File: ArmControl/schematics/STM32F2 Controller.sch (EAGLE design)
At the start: 87 parts, among them IC1 REG1117, IC2 TL072D, IC3 TL072D, Q301 BC846, Q701 BC846, U1 STM32F10XRXT6

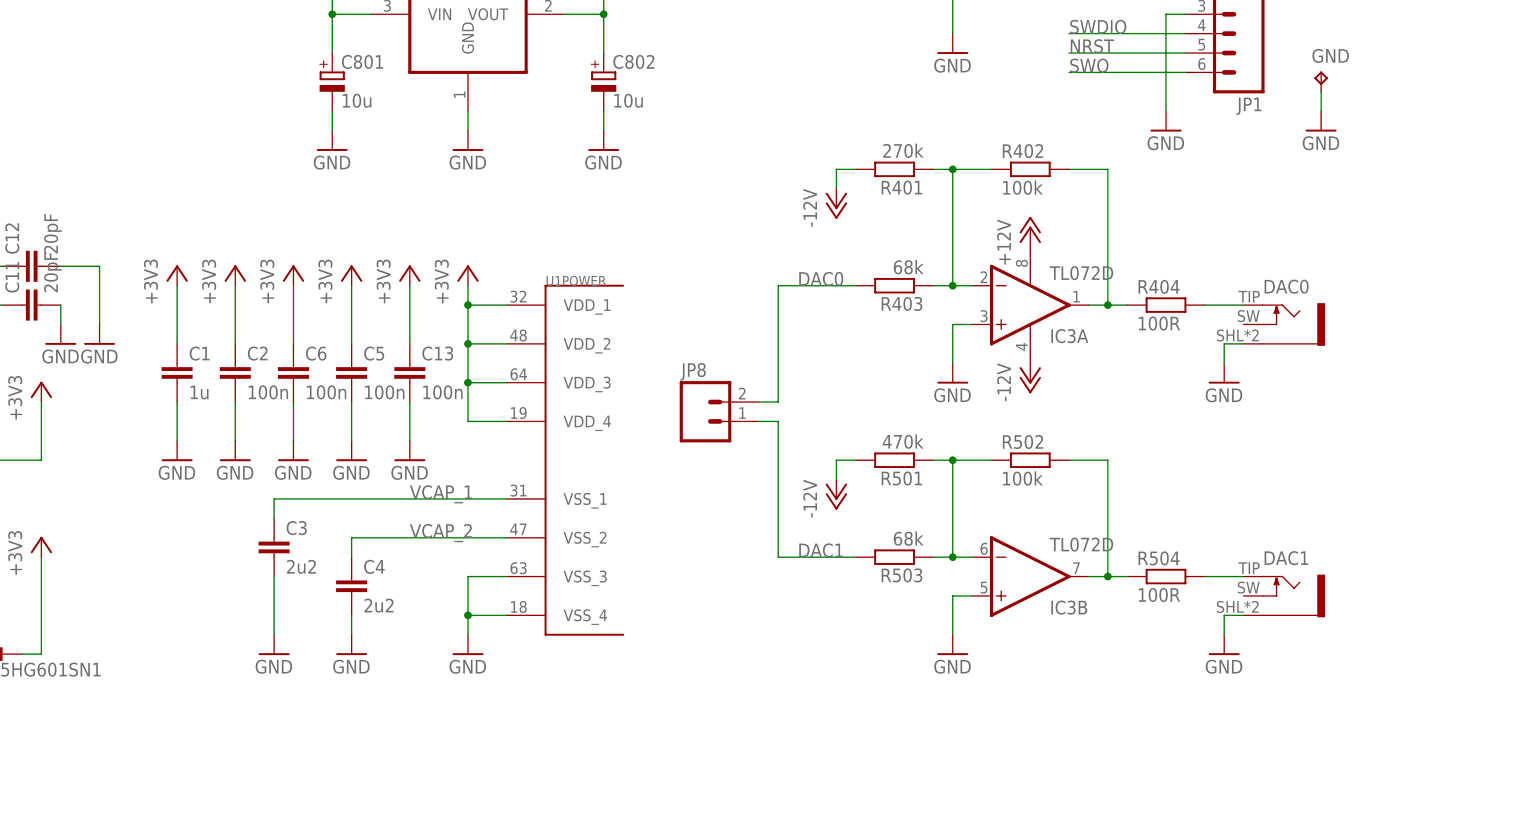
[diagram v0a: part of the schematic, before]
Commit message: rerouted pc0-pc3
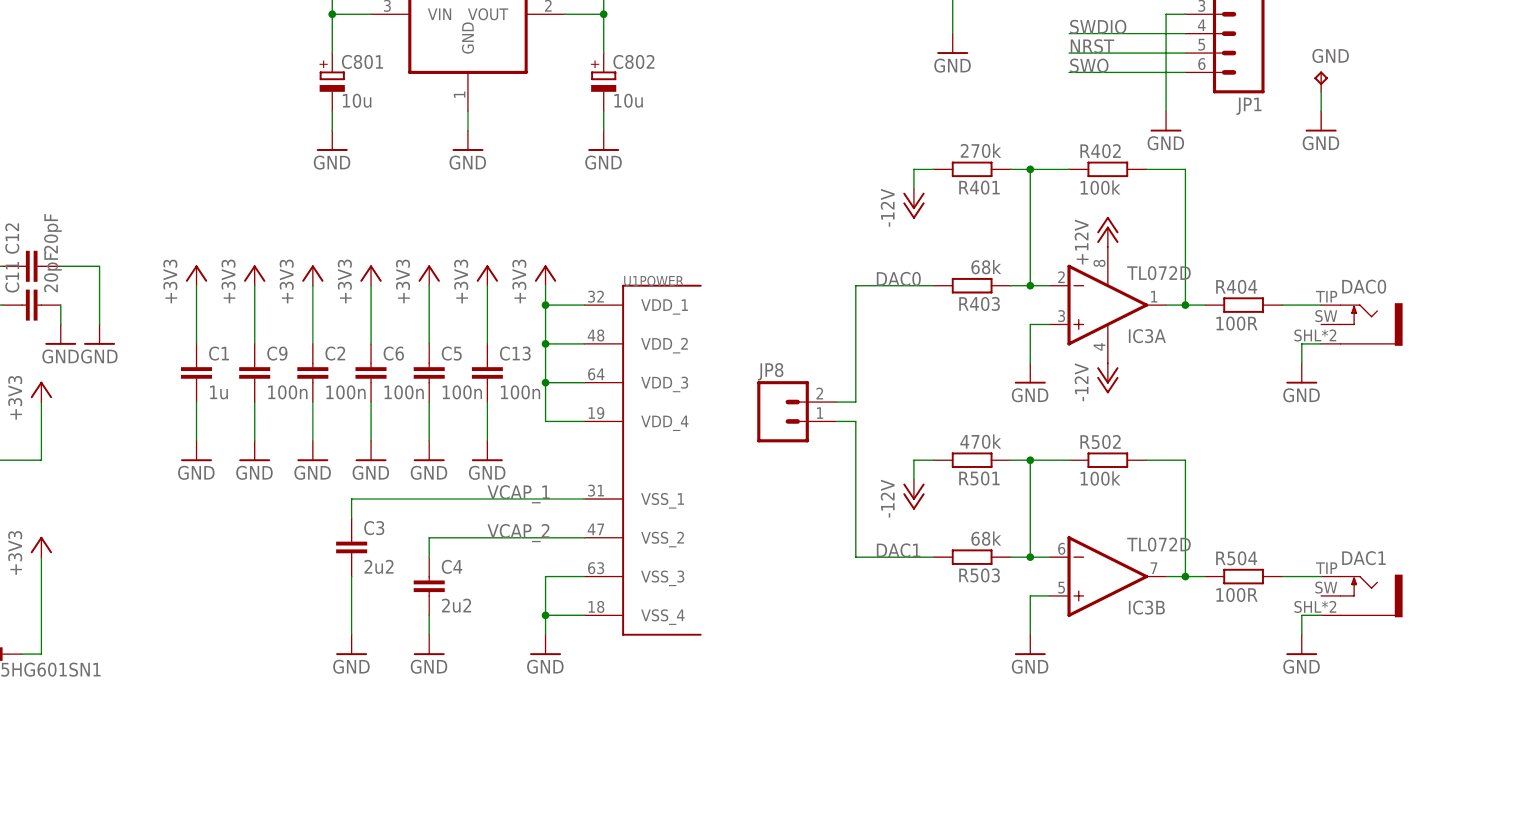
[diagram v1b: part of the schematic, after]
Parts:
- added C9: 100n, resistor:C-EUC0603
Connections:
- net +3V3: now also C9.1
- net GND: now also C9.2
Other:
- moved on the sheet: C1, C13, C2, C3, C4, C5, C6, DAC0, DAC1, IC3A, IC3B, JP8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

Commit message: removed usb connector, inserted jack headers, routed
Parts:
- removed D801: (no value), SparkFun:DIODESMA
- removed GND: TPPAD1-20, testpad:TPPAD1-20
- removed R801, R802: 22R, resistor:R-EU_R0603
- removed R803: 100k, resistor:R-EU_R0603
- removed U$3: USB-MINIB-5PIN, SparkFun:USB-MINIB-5PIN
- added JP11, JP12, JP13, JP14, JP15, JP16, JP17, JP18, JP19, JP20, JP21, JP22, JP23: (no value), SparkFun:M02PTH
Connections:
- removed net DM: R801.1, U$3.D-
- removed net DP: R802.1, U$3.D+
- new net N$10: DGO0.SW, JP11.1
- new net N$11: DGO0.TIP, JP11.2
- new net N$22: DGI0.SW, JP14.1
- new net N$23: DGI0.TIP, JP14.2
- new net N$24: ADC1.SW, JP16.1
- new net N$25: ADC1.TIP, JP16.2
- new net N$26: JP17.2, R203.1
- new net N$29: DAC1.SW, JP20.1
- new net N$30: DAC1.TIP, JP20.2
- new net N$31: JP18.1, R404.2
- new net N$32: JP18.2, R504.2
- net +12V: now also JP23.1
- net +3V3: now also JP21.1
- net +5V: now also JP22.1; no longer D801.C
- net -12V: now also JP23.2
- net DI0: now also JP12.2
- net DO0: now also JP13.1
- net GND: now also JP21.2, JP22.2; no longer ADC0.SW, ADC1.SW, DGI0.SW, GND.TP, R803.2, U$3.GND, U$3.MTN1, U$3.MTN2, U$3.MTN3, U$3.MTN4
- net N$1: now also ADC0.SW, JP15.1; no longer ADC1.TIP, R103.1
- net N$17: now also JP15.2; no longer R203.1
- net N$21: now also JP12.1, R301.1; no longer R803.1, U$3.ID
- net N$28: now also JP17.1, R103.1; no longer DGI0.TIP, R301.1
- net N$35: now also JP13.2; no longer DGO0.TIP
- net N$8: now also DAC0.SW, JP19.1; no longer DAC0.TIP, R404.2
- net N$9: now also DAC0.TIP, JP19.2; no longer DAC1.TIP, R504.2
- net PA11: no longer R801.2
- net PA12: no longer R802.2
- net PA9: no longer D801.A, U$3.VBUS
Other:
- moved on the sheet: ADC0, ADC1, DAC0, DAC1, DGI0, DGO0

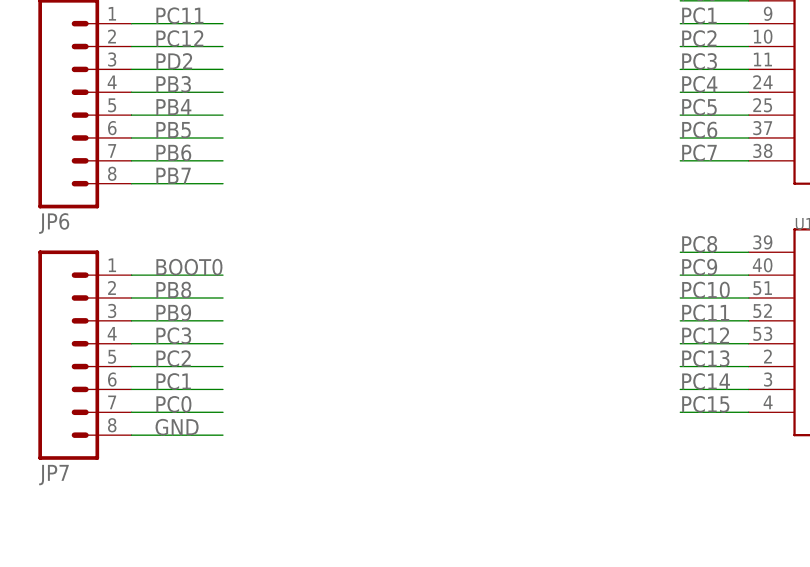
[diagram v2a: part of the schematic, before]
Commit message: added header for PC13-PC15
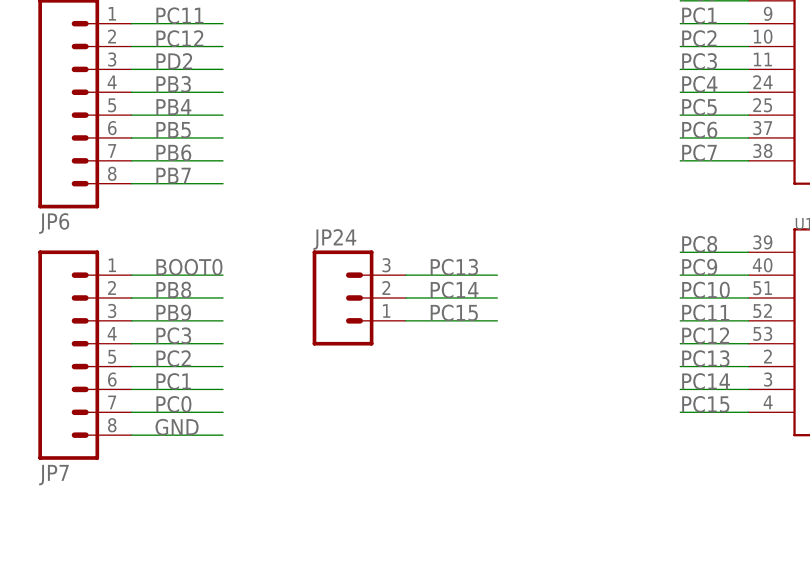
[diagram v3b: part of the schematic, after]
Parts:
- added JP24: (no value), SparkFun:M03PTH
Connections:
- net PC13: now also JP24.3
- net PC14: now also JP24.2
- net PC15: now also JP24.1
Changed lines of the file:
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@@
 <part name="P-8" library="supply1" deviceset="-12V" device=""/>
 <part name="P+8" library="supply1" deviceset="+12V" device=""/>
+<part name="JP24" library="SparkFun" deviceset="M03" device="PTH"/>
 </parts>
 <sheets>
@@
 <instance part="P-8" gate="1" x="355.6" y="55.88"/>
 <instance part="P+8" gate="1" x="355.6" y="73.66"/>
+<instance part="JP24" gate="G$1" x="-7.62" y="-17.78"/>
 </instances>
 <busses>
@@
 <pinref part="U1" gate="PORTC_H" pin="PC13"/>
 </segment>
+<segment>
+<pinref part="JP24" gate="G$1" pin="3"/>
+<wire x1="0" y1="-15.24" x2="10.16" y2="-15.24" width="0.1524" layer="91"/>
+<label x="2.54" y="-15.24" size="1.778" layer="95"/>
+</segment>
 </net>
 <net name="PC15" class="0">
@@
 <label x="30.48" y="-30.48" size="1.778" layer="95"/>
 <pinref part="U1" gate="PORTC_H" pin="PC15"/>
+</segment>
+<segment>
+<pinref part="JP24" gate="G$1" pin="1"/>
+<wire x1="0" y1="-20.32" x2="10.16" y2="-20.32" width="0.1524" layer="91"/>
+<label x="2.54" y="-20.32" size="1.778" layer="95"/>
 </segment>
 </net>
@@
 <pinref part="U1" gate="PORTC_H" pin="PC14"/>
 </segment>
-</net>
+<segment>
+<pinref part="JP24" gate="G$1" pin="2"/>
+<wire x1="0" y1="-17.78" x2="10.16" y2="-17.78" width="0.1524" layer="91"/>
+<label x="2.54" y="-17.78" size="1.778" layer="95"/>
+</segment>
+</net>

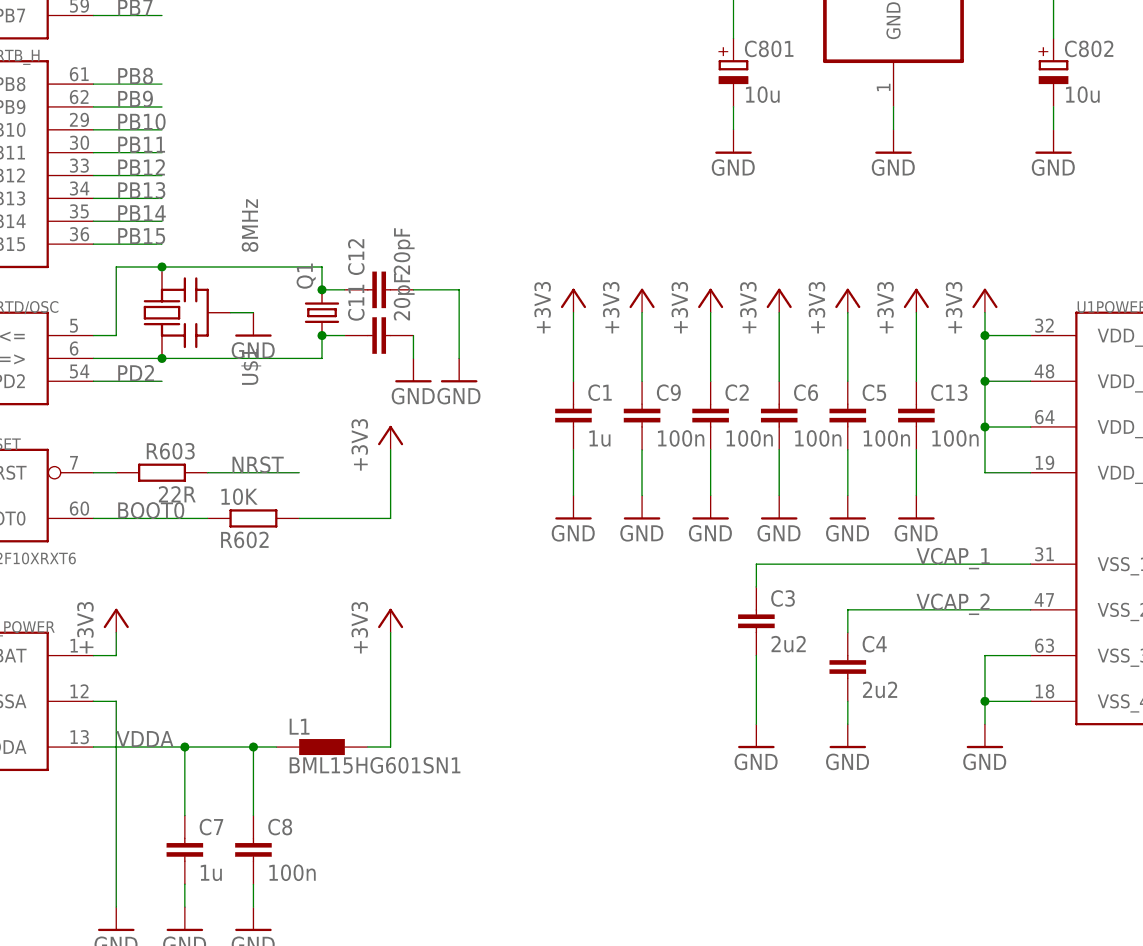
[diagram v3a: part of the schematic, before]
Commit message: added and layed out labels
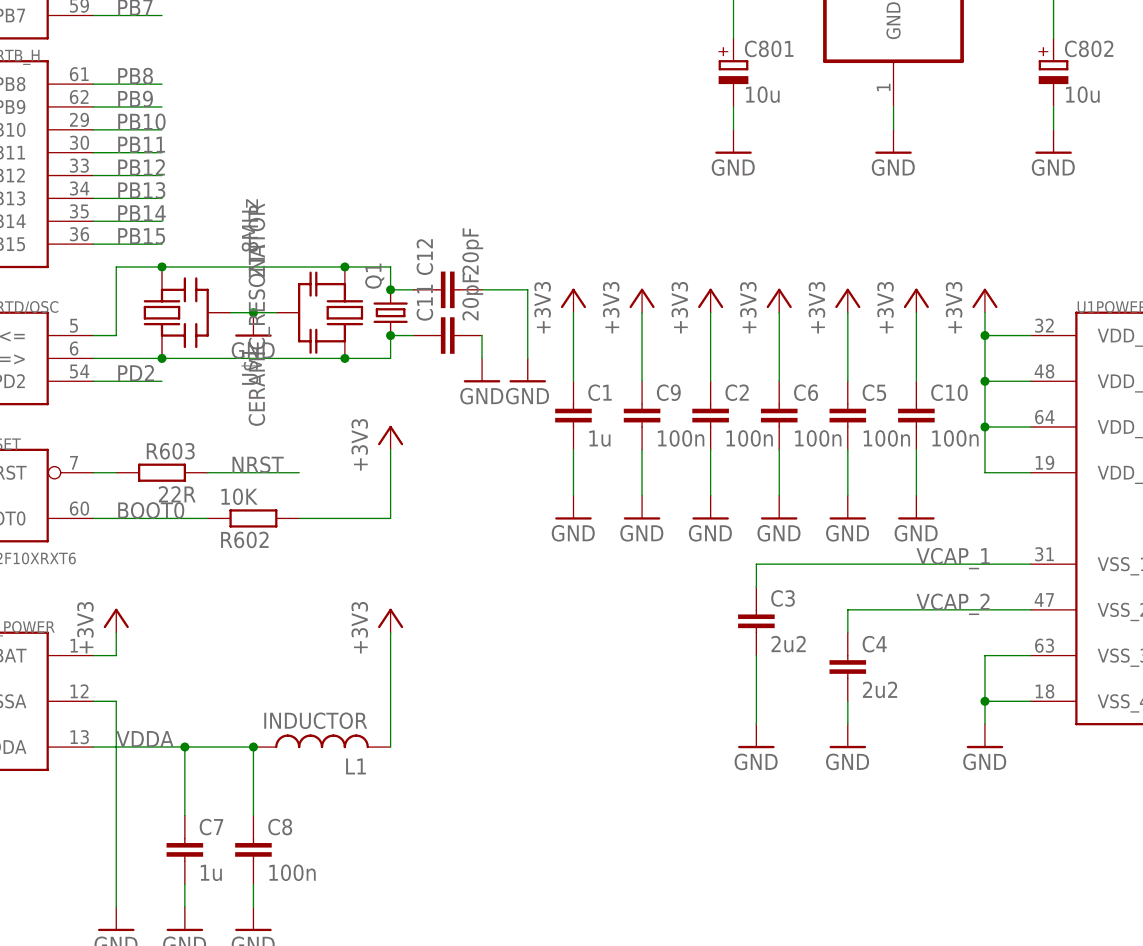
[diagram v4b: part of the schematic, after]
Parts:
- added ZTT: CERAMIC_RESONATOR, Rebel:CERAMIC_RESONATOR
- L1: value BML15HG601SN1 -> INDUCTOR; device inductors:BML15HG601SN1 -> Rebel:INDUCTOR
- renumbered C13 to C10
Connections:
- net GND: now also ZTT.GND
- net N$19: now also ZTT.IN
- net N$20: now also ZTT.OUT
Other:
- moved on the sheet: C11, C12, Q1
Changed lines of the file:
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@@
 <part name="R602" library="resistor" deviceset="R-EU_" device="R0603" value="10K"/>
 <part name="GND7" library="supply1" deviceset="GND" device=""/>
-<part name="L1" library="inductors" deviceset="BML15H" device="" technology="G601SN1"/>
+<part name="L1" library="Rebel" deviceset="INDUCTOR" device=""/>
 <part name="+3V3" library="supply1" deviceset="+3V3" device=""/>
 <part name="+3V4" library="supply1" deviceset="+3V3" device=""/>
@@
 <part name="C4" library="resistor" deviceset="C-EU" device="C0603" value="2u2"/>
 <part name="C7" library="resistor" deviceset="C-EU" device="C0603" value="1u"/>
-<part name="C13" library="resistor" deviceset="C-EU" device="C0603" value="100n"/>
+<part name="C10" library="resistor" deviceset="C-EU" device="C0603" value="100n"/>
 <part name="+3V15" library="supply1" deviceset="+3V3" device=""/>
 <part name="GND43" library="supply1" deviceset="GND" device=""/>
@@
 <part name="P+8" library="supply1" deviceset="+12V" device=""/>
 <part name="JP24" library="SparkFun" deviceset="M03" device="PTH"/>
+<part name="ZTT" library="Rebel" deviceset="CERAMIC_RESONATOR" device=""/>
 </parts>
 <sheets>
@@
 <instance part="U$1" gate="G$1" x="101.6" y="17.78" rot="R90"/>
 <instance part="GND23" gate="1" x="106.68" y="15.24"/>
-<instance part="Q1" gate="G$1" x="114.3" y="17.78" rot="R90"/>
-<instance part="C11" gate="G$1" x="119.38" y="15.24" rot="R90"/>
-<instance part="C12" gate="G$1" x="119.38" y="20.32" rot="R90"/>
-<instance part="GND24" gate="1" x="124.46" y="10.16"/>
-<instance part="GND25" gate="1" x="129.54" y="10.16"/>
+<instance part="Q1" gate="G$1" x="121.92" y="17.78" rot="R90"/>
+<instance part="C11" gate="G$1" x="127" y="15.24" rot="R90"/>
+<instance part="C12" gate="G$1" x="127" y="20.32" rot="R90"/>
+<instance part="GND24" gate="1" x="132.08" y="10.16"/>
+<instance part="GND25" gate="1" x="137.16" y="10.16"/>
 <instance part="JP3" gate="G$1" x="-35.56" y="60.96" rot="MR180"/>
 <instance part="JP2" gate="G$1" x="-5.08" y="60.96" rot="MR180"/>
@@
 <instance part="C4" gate="G$1" x="172.72" y="-20.32"/>
 <instance part="C7" gate="G$1" x="99.06" y="-40.64"/>
-<instance part="C13" gate="G$1" x="180.34" y="7.62"/>
+<instance part="C10" gate="G$1" x="180.34" y="7.62"/>
 <instance part="+3V15" gate="G$1" x="180.34" y="20.32"/>
 <instance part="GND43" gate="1" x="180.34" y="-5.08"/>
@@
 <instance part="P+8" gate="1" x="355.6" y="73.66"/>
 <instance part="JP24" gate="G$1" x="-7.62" y="-17.78"/>
+<instance part="ZTT" gate="G$1" x="114.3" y="17.78" rot="R270"/>
 </instances>
 <busses>
@@
 <pinref part="GND23" gate="1" pin="GND"/>
 <wire x1="104.14" y1="17.78" x2="106.68" y2="17.78" width="0.1524" layer="91"/>
+<pinref part="ZTT" gate="G$1" pin="GND"/>
+<wire x1="109.22" y1="17.78" x2="106.68" y2="17.78" width="0.1524" layer="91"/>
+<junction x="106.68" y="17.78"/>
 </segment>
 <segment>
 <pinref part="C11" gate="G$1" pin="2"/>
 <pinref part="GND24" gate="1" pin="GND"/>
-<wire x1="124.46" y1="15.24" x2="124.46" y2="12.7" width="0.1524" layer="91"/>
+<wire x1="132.08" y1="15.24" x2="132.08" y2="12.7" width="0.1524" layer="91"/>
 </segment>
 <segment>
 <pinref part="C12" gate="G$1" pin="2"/>
 <pinref part="GND25" gate="1" pin="GND"/>
-<wire x1="124.46" y1="20.32" x2="129.54" y2="20.32" width="0.1524" layer="91"/>
-<wire x1="129.54" y1="20.32" x2="129.54" y2="12.7" width="0.1524" layer="91"/>
+<wire x1="132.08" y1="20.32" x2="137.16" y2="20.32" width="0.1524" layer="91"/>
+<wire x1="137.16" y1="20.32" x2="137.16" y2="12.7" width="0.1524" layer="91"/>
 </segment>
 <segment>
@@
 </segment>
 <segment>
-<pinref part="C13" gate="G$1" pin="2"/>
+<pinref part="C10" gate="G$1" pin="2"/>
 <pinref part="GND43" gate="1" pin="GND"/>
 <wire x1="180.34" y1="2.54" x2="180.34" y2="-2.54" width="0.1524" layer="91"/>
@@
 <pinref part="L1" gate="G$1" pin="2"/>
 <pinref part="+3V3" gate="G$1" pin="+3V3"/>
-<wire x1="119.38" y1="-30.48" x2="121.92" y2="-30.48" width="0.1524" layer="91"/>
 <wire x1="121.92" y1="-30.48" x2="121.92" y2="-17.78" width="0.1524" layer="91"/>
 </segment>
@@
 <segment>
 <pinref part="+3V15" gate="G$1" pin="+3V3"/>
-<pinref part="C13" gate="G$1" pin="1"/>
+<pinref part="C10" gate="G$1" pin="1"/>
 <wire x1="180.34" y1="17.78" x2="180.34" y2="10.16" width="0.1524" layer="91"/>
 </segment>
@@
 <wire x1="88.9" y1="-30.48" x2="99.06" y2="-30.48" width="0.1524" layer="91"/>
 <wire x1="99.06" y1="-30.48" x2="106.68" y2="-30.48" width="0.1524" layer="91"/>
-<wire x1="106.68" y1="-30.48" x2="109.22" y2="-30.48" width="0.1524" layer="91"/>
 <wire x1="99.06" y1="-38.1" x2="99.06" y2="-30.48" width="0.1524" layer="91"/>
 <junction x="99.06" y="-30.48"/>
@@
 <wire x1="91.44" y1="22.86" x2="96.52" y2="22.86" width="0.1524" layer="91"/>
 <pinref part="Q1" gate="G$1" pin="2"/>
-<wire x1="96.52" y1="22.86" x2="114.3" y2="22.86" width="0.1524" layer="91"/>
-<wire x1="114.3" y1="22.86" x2="114.3" y2="20.32" width="0.1524" layer="91"/>
+<wire x1="96.52" y1="22.86" x2="116.84" y2="22.86" width="0.1524" layer="91"/>
+<wire x1="116.84" y1="22.86" x2="121.92" y2="22.86" width="0.1524" layer="91"/>
+<wire x1="121.92" y1="22.86" x2="121.92" y2="20.32" width="0.1524" layer="91"/>
 <junction x="96.52" y="22.86"/>
 <pinref part="C12" gate="G$1" pin="1"/>
-<wire x1="116.84" y1="20.32" x2="114.3" y2="20.32" width="0.1524" layer="91"/>
-<junction x="114.3" y="20.32"/>
+<wire x1="124.46" y1="20.32" x2="121.92" y2="20.32" width="0.1524" layer="91"/>
+<junction x="121.92" y="20.32"/>
+<pinref part="ZTT" gate="G$1" pin="IN"/>
+<junction x="116.84" y="22.86"/>
 </segment>
 </net>
@@
 <pinref part="U1" gate="PORTD/OSC" pin="PD1/OSC=&gt;"/>
 <pinref part="Q1" gate="G$1" pin="1"/>
-<wire x1="96.52" y1="12.7" x2="114.3" y2="12.7" width="0.1524" layer="91"/>
-<wire x1="114.3" y1="12.7" x2="114.3" y2="15.24" width="0.1524" layer="91"/>
+<wire x1="96.52" y1="12.7" x2="116.84" y2="12.7" width="0.1524" layer="91"/>
+<wire x1="116.84" y1="12.7" x2="121.92" y2="12.7" width="0.1524" layer="91"/>
+<wire x1="121.92" y1="12.7" x2="121.92" y2="15.24" width="0.1524" layer="91"/>
 <junction x="96.52" y="12.7"/>
 <pinref part="C11" gate="G$1" pin="1"/>
-<wire x1="116.84" y1="15.24" x2="114.3" y2="15.24" width="0.1524" layer="91"/>
-<junction x="114.3" y="15.24"/>
-</segment>
-</net>
+<wire x1="124.46" y1="15.24" x2="121.92" y2="15.24" width="0.1524" layer="91"/>
+<junction x="121.92" y="15.24"/>
+<pinref part="ZTT" gate="G$1" pin="OUT"/>
+<junction x="116.84" y="12.7"/>
+</segment>
+</net>
